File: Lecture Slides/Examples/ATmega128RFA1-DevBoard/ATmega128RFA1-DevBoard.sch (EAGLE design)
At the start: 51 parts, among them J1 ISP, J2 ARDUINO_UNO_R3, J3 POWER_JACKPTH_LOCK, U1 ATMEGA128RFA1, U2 LM1117, Y1 16MHz, Y2 32.768kHz

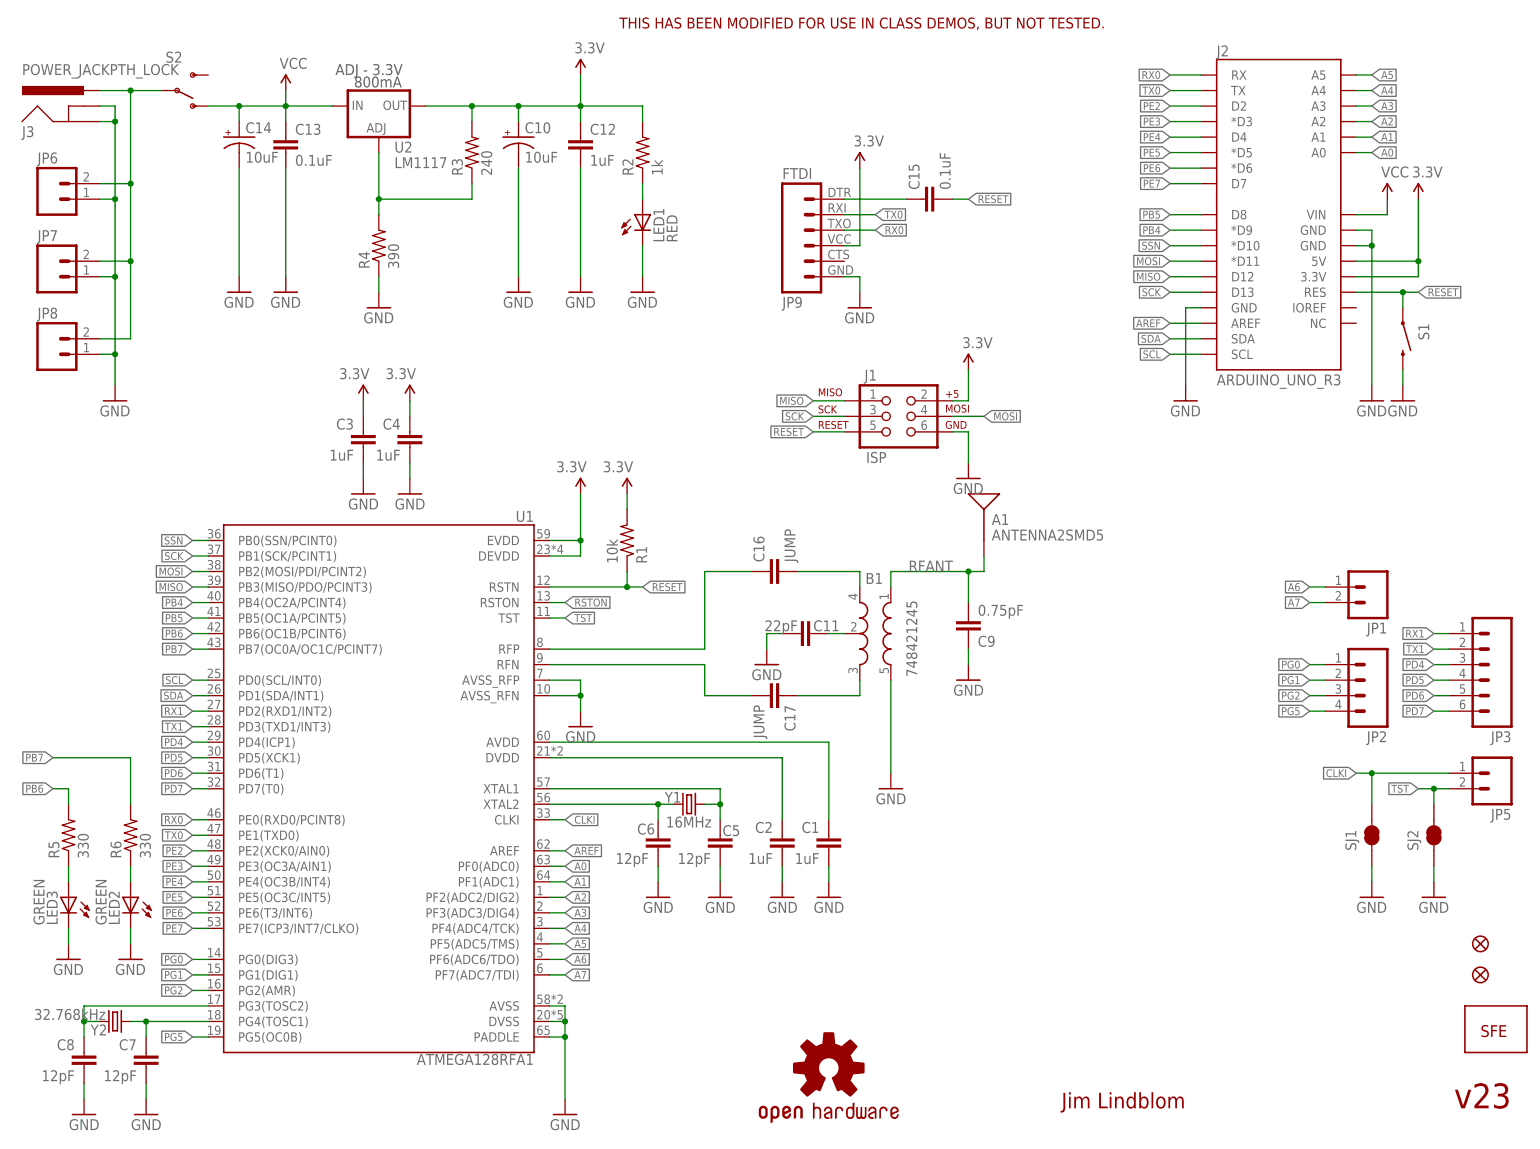
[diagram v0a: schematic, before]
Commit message: examples for board layout/placement
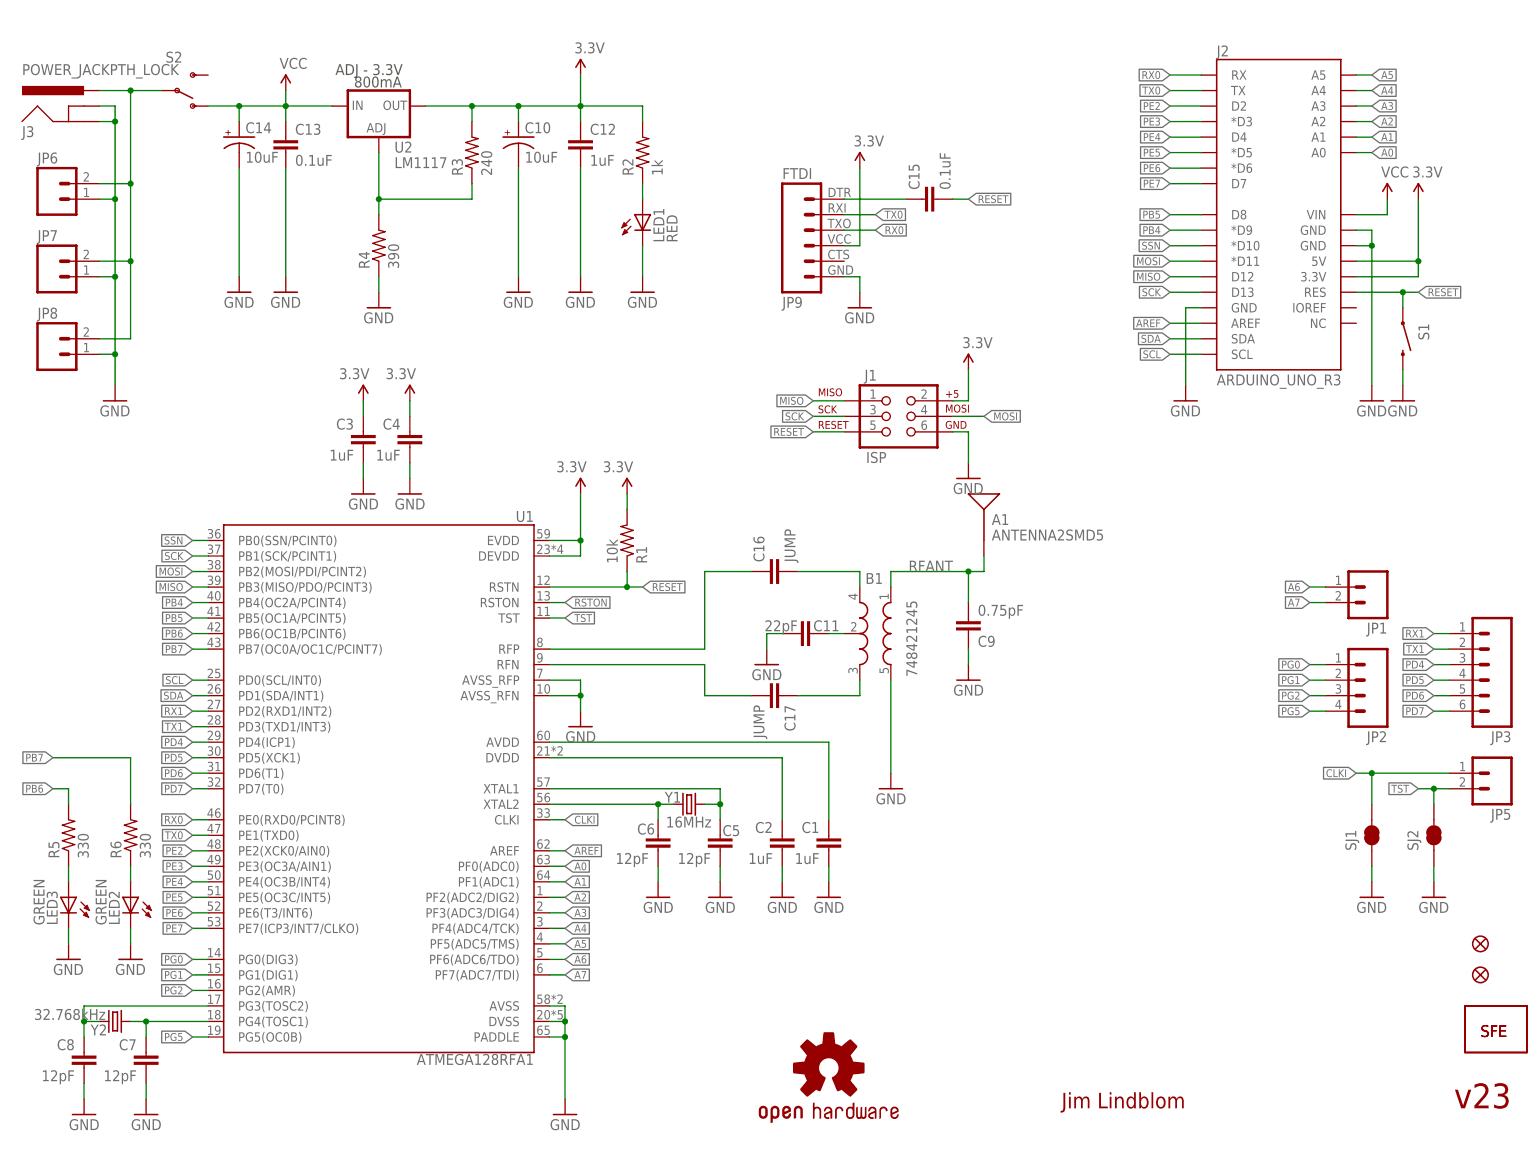
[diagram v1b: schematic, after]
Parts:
- added JP10: LOGO-SFENEW, SparkFun-Aesthetics:LOGO-SFENEW
- A1: device ATmega128RFA1-DevBoard.lbr:ANTENNA2SMD5 -> SparkFun-RF:ANTENNA2SMD5
- B1: device ATmega128RFA1-DevBoard.lbr:BALUN0805 -> SparkFun-RF:BALUN0805
- C1, C11, C12, C13, C15, C2, C3, C4, C5, C6, C7, C8, C9: device ATmega128RFA1-DevBoard.lbr:CAP0402-CAP -> SparkFun-Passives:CAP0402-CAP
- C10, C14: device ATmega128RFA1-DevBoard.lbr:CAP_POL1206 -> SparkFun-Passives:CAP_POL1206
- C16, C17: device ATmega128RFA1-DevBoard.lbr:CAP0402-CAP -> SparkFun:CAP0402-CAP
- FID1, FID2: device ATmega128RFA1-DevBoard.lbr:FIDUCIALUFIDUCIAL -> SparkFun-Aesthetics:FIDUCIALUFIDUCIAL
- J1: device ATmega128RFA1-DevBoard.lbr:AVR_SPI_PRG_6NS -> SparkFun-Connectors:AVR_SPI_PRG_6NS
- J2: device ATmega128RFA1-DevBoard.lbr:ARDUINO_UNO_R3 -> SparkFun-Boards:ARDUINO_UNO_R3
- J3: device ATmega128RFA1-DevBoard.lbr:POWER_JACKPTH_LOCK -> SparkFun-Connectors:POWER_JACKPTH_LOCK
- JP1, JP5, JP7: device ATmega128RFA1-DevBoard.lbr:M021X02_NO_SILK -> SparkFun-Connectors:M021X02_NO_SILK
- JP2: device ATmega128RFA1-DevBoard.lbr:M041X04_NO_SILK -> SparkFun-Connectors:M041X04_NO_SILK
- JP3: device ATmega128RFA1-DevBoard.lbr:M06SIP-NS -> SparkFun-Connectors:M06SIP-NS
- JP4: device ATmega128RFA1-DevBoard.lbr:LOGO-SFENEW -> SparkFun-Aesthetics:LOGO-SFENEW
- JP6: device ATmega128RFA1-DevBoard.lbr:M02JST-PTH-2 -> SparkFun-Connectors:M02JST-PTH-2
- JP8: device ATmega128RFA1-DevBoard.lbr:M023.5MM-NO_SILK -> SparkFun-Connectors:M023.5MM-NO_SILK
- JP9: device ATmega128RFA1-DevBoard.lbr:FTDI_BASICPTH -> SparkFun-Connectors:FTDI_BASICPTH
- LED1, LED2, LED3: device ATmega128RFA1-DevBoard.lbr:LED0603 -> SparkFun-LED:LED0603
- R1, R2: device ATmega128RFA1-DevBoard.lbr:RESISTOR0402-RES -> SparkFun-Passives:RESISTOR0402-RES
- R3, R4, R5, R6: device ATmega128RFA1-DevBoard.lbr:RESISTOR0402-RES -> SparkFun:RESISTOR0402-RES
- S1: device ATmega128RFA1-DevBoard.lbr:SWITCH-MOMENTARY-2SMD -> SparkFun-Electromechanical:SWITCH-MOMENTARY-2SMD
- S2: device ATmega128RFA1-DevBoard.lbr:SWITCH-SPST-SMD-A -> SparkFun:SWITCH-SPST-SMD-A
- SJ1, SJ2: device ATmega128RFA1-DevBoard.lbr:SOLDERJUMPERTRACE -> SparkFun-Passives:SOLDERJUMPERTRACE
- U$1: device ATmega128RFA1-DevBoard.lbr:OSHW-LOGOS -> SparkFun-Aesthetics:OSHW-LOGOS
- U1: device ATmega128RFA1-DevBoard.lbr:ATMEGA128RFA1 -> SparkFun-DigitalIC:ATMEGA128RFA1
- U2: device ATmega128RFA1-DevBoard.lbr:V_REG_317SMD -> SparkFun:V_REG_317SMD
- Y1: device ATmega128RFA1-DevBoard.lbr:CRYSTAL5X3 -> SparkFun-FreqCtrl:CRYSTAL5X3
- Y2: device ATmega128RFA1-DevBoard.lbr:CRYSTAL32-SMD -> SparkFun-FreqCtrl:CRYSTAL32-SMD
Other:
- note removed: "THIS HAS BEEN MODIFIED FOR USE IN CLASS DEMOS, BUT NOT TESTED."
